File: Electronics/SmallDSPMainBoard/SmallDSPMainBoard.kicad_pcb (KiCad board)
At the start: 2 copper layers, 209 parts, among them J1 Header, J10 Programming, J11 NC3FAAH2, J12 NC3FAAH2, J13 NC3MAAH, J14 NC3MAAH, J15 Barrel_Jack_Switch, J16 Header, J2 Header, J3 Header, J4 Header, J5 Header, J6 Header, J7 Header, J8 Header, J9 Header, Q1 NSS1C300ET4, SW1 TS-1187A-B-A-B, SW2 CJS-1201TB, U1 ADAU1463, U10 NE5532, U11 NE5532, U12 L7805, U13 TLV76133, U2 ADM811, U3 M95M01-R, U4 NE5532, U5 NE5532, U6 NE5532, U7 PCM1808, U8 PCM1754, U9 NE5532, Y1 830105957509

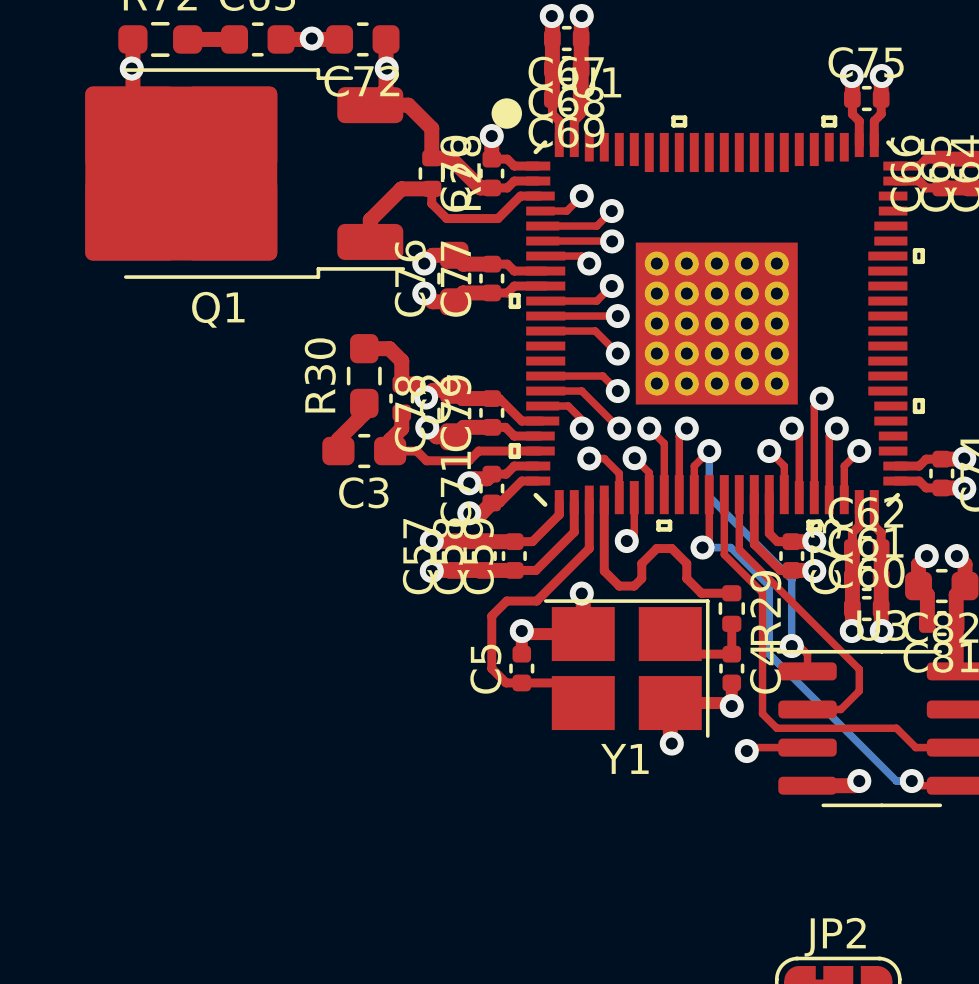
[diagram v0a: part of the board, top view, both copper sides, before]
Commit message: Adds seperate ground for crystal and pll
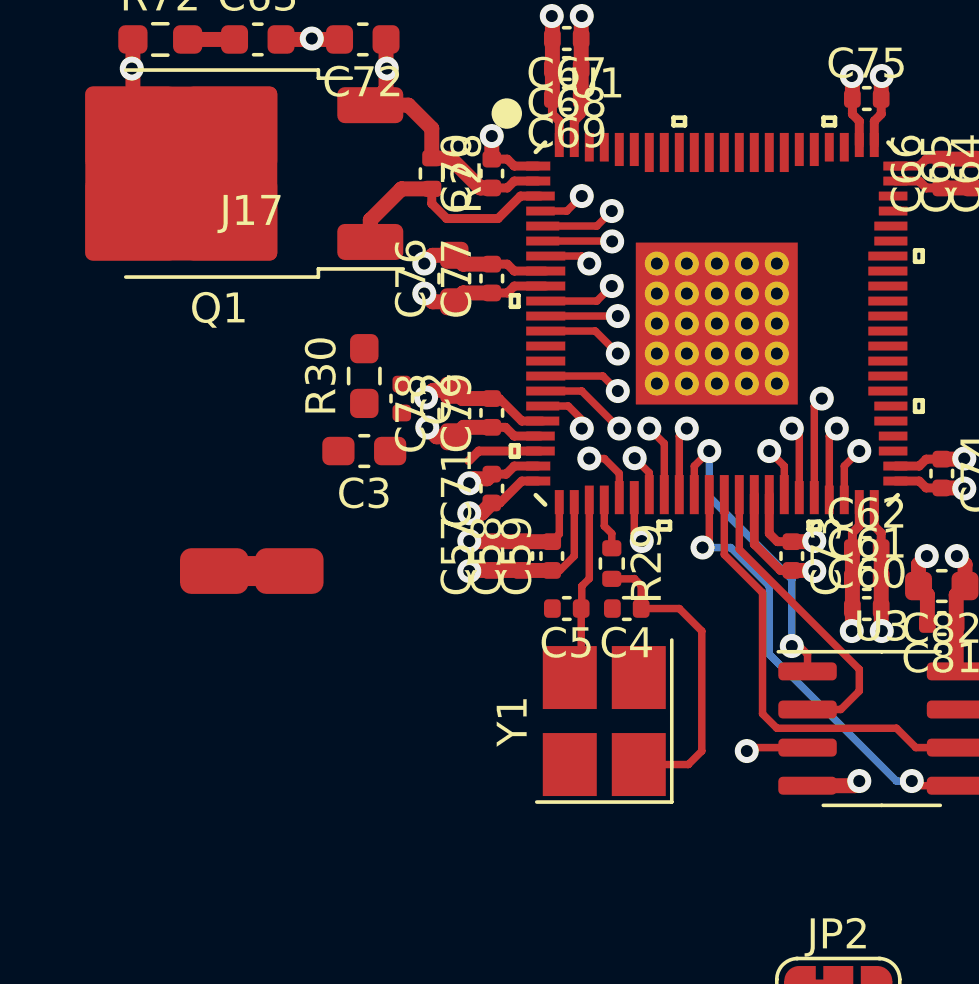
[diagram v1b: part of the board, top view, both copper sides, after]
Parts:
- added J17: ~, 1_Project_Footprints:Short, F.Cu at (123.8, 143.2)
- moved R29 4.27 mm to (135.8, 143.0)
- moved C4 4.03 mm to (136.2, 144.5), turned to 180 degrees
- moved C5 2.50 mm to (134.2, 144.5), turned to 180 degrees
- moved Y1 1.90 mm to (135.5, 148.2), turned to 90 degrees
- moved C57 1.25 mm to (131.8, 142.8)
- moved C58 1.25 mm to (132.8, 142.8)
- moved C59 1.25 mm to (133.8, 142.8)
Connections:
- C2 pad 1: GND -> GND1
- C78 pad 2: GND -> GND1
- C79 pad 2: GND -> GND1
- R30 pad 2: GND -> GND1
- U1 pad 18: GND -> GND1
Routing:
- net GND: track 127.9 -> 111.0 mm, vias 74 -> 69
- net Net-(C4-Pad1): track 3.34 -> 10.5 mm
- net Net-(U1A-Xtal_Out): track 8.55 -> 1.72 mm
- net Net-(U1A-Xtal_In/MCLK_In): track 11.1 -> 6.19 mm
- net GND1: track 0.00 -> 4.41 mm, vias 0 -> 1
- net Net-(U1A-PLLFlt): track 6.71 -> 2.52 mm
- net Net-(C3-Pad2): track 1.94 -> 0.00 mm
- net +1V2: track 22.5 -> 21.7 mm

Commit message: Partly finishes layout
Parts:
- removed J17: ~, 1_Project_Footprints:Short
- removed the R1 at (153.5, 105.5)
- removed the R10 at (156.4, 111.5)
- removed the R11 at (159.3, 101.5)
- removed the R12 at (159.3, 103.5)
- removed the R2 at (153.5, 107.5)
- removed the R3 at (153.5, 109.5)
- removed the R4 at (153.5, 111.5)
- removed the R5 at (156.4, 101.5)
- removed the R6 at (156.4, 103.5)
- removed the R7 at (156.4, 105.5)
- removed the R8 at (156.4, 107.5)
- removed the R9 at (156.4, 109.5)
- added R40: 100R, Resistor_SMD:R_0402_1005Metric, F.Cu at (75.0, 89.2)
- added R41: 100R, Resistor_SMD:R_0402_1005Metric, F.Cu at (76.0, 89.2)
- added R42: 100R, Resistor_SMD:R_0402_1005Metric, F.Cu at (77.0, 89.2)
- added R43: 4k7, Resistor_SMD:R_0402_1005Metric, F.Cu at (73.3, 67.5)
- J1: renamed from J2; moved to B.Cu
- J10: renamed from J1; moved to B.Cu
- J2: renamed from J3; moved to B.Cu
- J3: renamed from J16; moved to B.Cu
- J4: renamed from J5; moved to B.Cu
- J5: renamed from J4; moved to B.Cu
- J6, J7, J8, J9: moved to B.Cu
- moved J3 178.8 mm to (90.0, 56.5), turned to 180 degrees
- moved J11 146.7 mm to (124.8, 73.9)
- moved J5 140.4 mm to (81.5, 83.2)
- moved J8 139.2 mm to (118.0, 67.5), turned to 180 degrees
- moved J2 129.5 mm to (89.5, 101.2)
- moved J4 122.9 mm to (115.8, 96.2), turned to 180 degrees
- moved C33 107.3 mm to (60.2, 17.9)
- moved C34 107.3 mm to (60.2, 58.0)
- moved C36 107.3 mm to (57.5, 15.9)
- moved C37 107.3 mm to (57.5, 51.5)
- moved C38 107.3 mm to (58.5, 13.4)
- moved C39 107.3 mm to (58.5, 54.0)
- moved C40 107.3 mm to (50.2, 16.2)
- moved C41 107.3 mm to (50.2, 51.2)
- moved C42 107.3 mm to (53.5, 15.7)
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- renumbered C7 to C10, C8 to C11, C9 to C12, C10 to C13, C11 to C14, C12 to C15, C13 to C16, C14 to C17, C15 to C18, C16 to C19, C80 to C2, C17 to C20, C18 to C21, C19 to C22, C20 to C23, C21 to C24, C22 to C25, C23 to C26, C24 to C27, C25 to C28, C26 to C29, C2 to C3, C27 to C30, C28 to C31, C29 to C32, C30 to C33, C31 to C34, C32 to C35, C33 to C36, C34 to C37, C35 to C38, C36 to C39, C3 to C4, C37 to C40, C38 to C41, C39 to C42, C40 to C43, C41 to C44, C42 to C45, C43 to C46, C44 to C47, C45 to C48, C46 to C49, C4 to C5, C47 to C50, C48 to C51, C49 to C52, C50 to C53, C51 to C54, C52 to C55, C53 to C56, C54 to C57, C55 to C58, C56 to C59, C5 to C6, C57 to C60, C58 to C61, C59 to C62, C60 to C63, C61 to C64, C62 to C65, C63 to C66, C64 to C67, C65 to C68, C66 to C69, C81 to C7, C67 to C70, C68 to C71, C69 to C72, C70 to C73, C71 to C74, C72 to C75, C73 to C76, C74 to C77, C75 to C78, C76 to C79, C82 to C8, C77 to C80, C78 to C81, C79 to C82, C6 to C9, J10 to J11, J11 to J12, J12 to J13, J13 to J14, J14 to J15, J15 to J16, JP8 to JP5, JP9 to JP6, JP5 to JP7, JP6 to JP8, JP7 to JP9, R13 to R1, R22 to R10, R23 to R11, R24 to R12, R25 to R13, R26 to R14, R27 to R15, R28 to R16, R29 to R17, R30 to R18, R31 to R19, R14 to R2, R32 to R20, R33 to R21, R34 to R22, R35 to R23, R36 to R24, R37 to R25, R38 to R26, R39 to R27, R40 to R28, R41 to R29, R15 to R3, R42 to R30, R43 to R31, R44 to R32, R45 to R33, R46 to R34, R47 to R35, R48 to R36, R49 to R37, R50 to R38, R51 to R39, R16 to R4, R52 to R44, R53 to R45, R54 to R46, R55 to R47, R56 to R48, R57 to R49, R17 to R5, R58 to R50, R59 to R51, R60 to R52, R61 to R53, R62 to R54, R63 to R55, R64 to R56, R65 to R57, R66 to R58, R67 to R59, R18 to R6, R68 to R60, R69 to R61, R70 to R62, R71 to R63, R72 to R64, R19 to R7, R20 to R8, R21 to R9
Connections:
- C3 pad 1: GND1 -> GND
- C81 pad 2: GND1 -> GND
- C82 pad 2: GND1 -> GND
- J2 pad 10: /SDATA_In3 -> /BCLK_In3
- J2 pad 14: /BCLK_In2 -> /SDATA_In2
- J2 pad 18: /SDATA_In2 -> /BCLK_In2
- J2 pad 6: /BCLK_In3 -> /SDATA_In3
- J3 pad 10: /SDATA_Out3 -> /LRCK_Out3
- J3 pad 13: /BCLK_Out1 -> /LRCK_Out1
- J3 pad 14: /BCLK_Out2 -> /SDATA_Out2
- J3 pad 15: /LRCK_Out1 -> /BCLK_Out1
- J3 pad 16: /LRCK_Out2 -> /BCLK_Out2
- J3 pad 18: /SDATA_Out2 -> /LRCK_Out2
- J3 pad 5: /BCLK_Out0 -> /LRCK_Out0
- J3 pad 6: /BCLK_Out3 -> /SDATA_Out3
- J3 pad 7: /LRCK_Out0 -> /BCLK_Out0
- J3 pad 8: /LRCK_Out3 -> /BCLK_Out3
- J5 pad 10: /SDATA_IO4 -> /SDATA_IO7
- J5 pad 3: /SDATA_IO0 -> /SDATA_IO3
- J5 pad 4: /SDATA_IO7 -> /SDATA_IO4
- J5 pad 5: /SDATA_IO1 -> /SDATA_IO2
- J5 pad 6: /SDATA_IO6 -> /SDATA_IO5
- J5 pad 7: /SDATA_IO2 -> /SDATA_IO1
- J5 pad 8: /SDATA_IO5 -> /SDATA_IO6
- J5 pad 9: /SDATA_IO3 -> /SDATA_IO0
- R18 pad 2: GND1 -> GND
- U1 pad 18: GND1 -> GND
- U1 pad 73: Net-(U1C-BCLK_In0) -> /BCLK_In0
- U1 pad 74: Net-(U1C-LRCK_In0/GPIO10) -> /LRCK_In0
- U1 pad 75: Net-(U1C-SDATA_In0) -> /SDATA_In0
- U1 pad 76: Net-(U1C-BCLK_In1) -> /BCLK_In1
- U1 pad 77: Net-(U1C-LRCK_In1/GPIO11) -> /LRCK_In1
- U1 pad 78: Net-(U1C-SDATA_In1) -> /SDATA_In1
- U1 pad 81: Net-(U1C-BCLK_In2) -> /BCLK_In2
- U1 pad 82: Net-(U1C-LRCK_In2/GPIO12) -> /LRCK_In2
- U1 pad 83: Net-(U1C-SDATA_In2) -> /SDATA_In2
- U1 pad 84: Net-(U1C-BCLK_In3) -> /BCLK_In3
- U1 pad 85: Net-(U1C-LRCK_In3/GPIO13) -> /LRCK_In3
- U1 pad 86: Net-(U1C-SDATA_In3) -> /SDATA_In3
- U7 pad 7: /LRCK_In0 -> Net-(U7-LRCK)
- U7 pad 8: /BCLK_In0 -> Net-(U7-BCLK)
- U7 pad 9: /SDATA_In0 -> Net-(U7-SDATA)
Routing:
- net /SDATA_IO0: track 0.00 -> 24.1 mm
- net /SDATA_IO1: track 0.00 -> 20.9 mm
- net /BCLK_In0: track 0.00 -> 20.7 mm
- net /LRCK_In0: track 0.00 -> 18.6 mm
- net /SDATA_IO2: track 0.00 -> 17.6 mm
- net /SDATA_In0: track 0.00 -> 16.5 mm
- net /SDATA_Out3: track 0.00 -> 15.0 mm
- net /SDATA_IO3: track 0.00 -> 14.5 mm
- net /SDATA_IO7: track 0.00 -> 14.0 mm
- net /SDATA_IO6: track 0.00 -> 13.7 mm
- net /SDATA_In3: track 0.00 -> 13.6 mm
- net /SDATA_IO5: track 0.00 -> 13.4 mm
- net /BCLK_In1: track 0.00 -> 13.2 mm
- net /SDATA_IO4: track 0.00 -> 13.1 mm
- net /BCLK_Out3: track 0.00 -> 13.0 mm
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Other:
- board outline added: 104 x 104 mm
